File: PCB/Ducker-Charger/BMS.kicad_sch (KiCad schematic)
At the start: 26 parts, among them Q5 NCE3080K, Q6 NCE3080K, U4 BQ7791500PWR

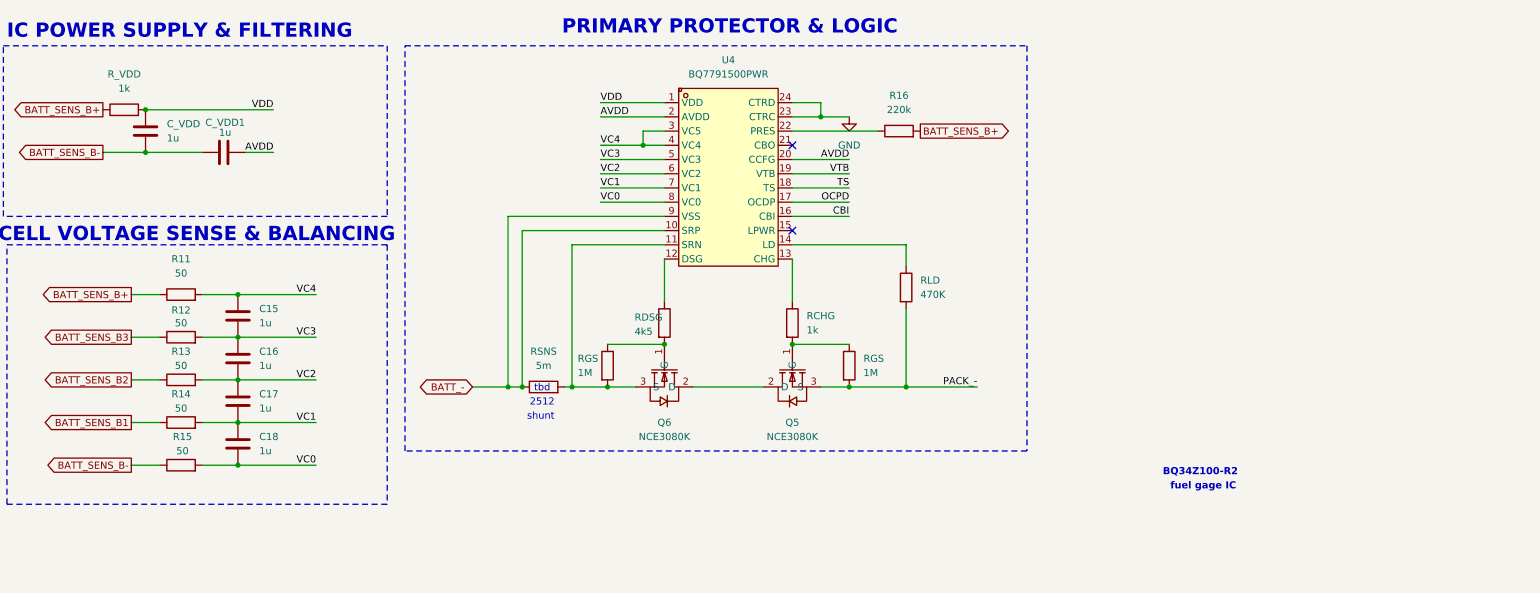
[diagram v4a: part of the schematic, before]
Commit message: fix: placement and values
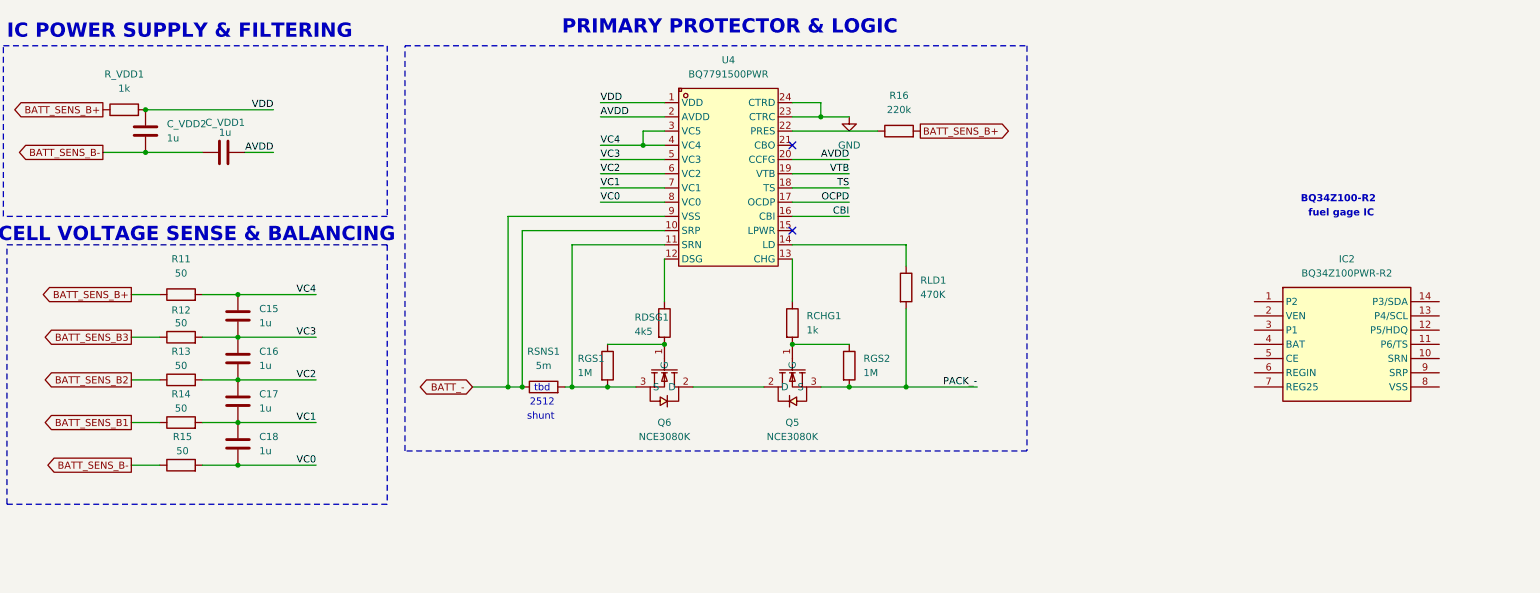
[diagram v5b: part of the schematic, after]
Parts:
- added IC2: BQ34Z100PWR-R2, SOP65P640X120-14N, symbol BQ34Z100PWR-R2:BQ34Z100PWR-R2
- renumbered C_VDD to C_VDD2, RCHG to RCHG1, RDSG to RDSG1, RGS to RGS1, RGS to RGS2, RLD to RLD1, RSNS to RSNS1, R_VDD to R_VDD1
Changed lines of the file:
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@@
 	(text "BQ34Z100-R2"
 		(exclude_from_sim no)
-		(at 229.108 107.95 0)
+		(at 253.746 59.182 0)
 		(effects
 			(font
@@
 	(text "fuel gage IC\n"
 		(exclude_from_sim no)
-		(at 229.616 110.49 0)
+		(at 254.254 61.722 0)
 		(effects
 			(font
@@
 		(dnp no)
 		(fields_autoplaced yes)
-		(property "Reference" "RSNS"
+		(property "Reference" "RSNS1"
 			(at 111.76 86.36 90)
 			(effects
@@
 			(project ""
 				(path "/74790d6c-a68e-4e6d-b4a9-43de1843f817/2619d069-74ef-4c2a-996f-0b2ab6b3180e"
-					(reference "RSNS")
+					(reference "RSNS1")
 					(unit 1)
 				)
@@
 		(dnp no)
 		(fields_autoplaced yes)
-		(property "Reference" "RGS"
+		(property "Reference" "RGS2"
 			(at 168.91 87.6299 0)
 			(effects
@@
 			(project "Ducker-Charger"
 				(path "/74790d6c-a68e-4e6d-b4a9-43de1843f817/2619d069-74ef-4c2a-996f-0b2ab6b3180e"
-					(reference "RGS")
+					(reference "RGS2")
 					(unit 1)
 				)
@@
 		(on_board yes)
 		(dnp no)
-		(property "Reference" "RDSG"
+		(property "Reference" "RDSG1"
 			(at 128.016 80.264 0)
 			(effects
@@
 			(project "Ducker-Charger"
 				(path "/74790d6c-a68e-4e6d-b4a9-43de1843f817/2619d069-74ef-4c2a-996f-0b2ab6b3180e"
-					(reference "RDSG")
+					(reference "RDSG1")
 					(unit 1)
 				)
@@
 		(dnp no)
 		(fields_autoplaced yes)
-		(property "Reference" "C_VDD"
+		(property "Reference" "C_VDD2"
 			(at 44.45 45.7199 0)
 			(effects
@@
 			(project "Ducker-Charger"
 				(path "/74790d6c-a68e-4e6d-b4a9-43de1843f817/2619d069-74ef-4c2a-996f-0b2ab6b3180e"
-					(reference "C_VDD")
+					(reference "C_VDD2")
 					(unit 1)
 				)
@@
 		(dnp no)
 		(fields_autoplaced yes)
-		(property "Reference" "RLD"
+		(property "Reference" "RLD1"
 			(at 179.07 73.6599 0)
 			(effects
@@
 			(project ""
 				(path "/74790d6c-a68e-4e6d-b4a9-43de1843f817/2619d069-74ef-4c2a-996f-0b2ab6b3180e"
-					(reference "RLD")
+					(reference "RLD1")
 					(unit 1)
 				)
@@
 		(dnp no)
 		(fields_autoplaced yes)
-		(property "Reference" "R_VDD"
+		(property "Reference" "R_VDD1"
 			(at 36.83 36.83 90)
 			(effects
@@
 			(project "Ducker-Charger"
 				(path "/74790d6c-a68e-4e6d-b4a9-43de1843f817/2619d069-74ef-4c2a-996f-0b2ab6b3180e"
-					(reference "R_VDD")
+					(reference "R_VDD1")
 					(unit 1)
 				)
@@
 	)
 	(symbol
+		(lib_id "BQ34Z100PWR-R2:BQ34Z100PWR-R2")
+		(at 238.76 77.47 0)
+		(unit 1)
+		(exclude_from_sim no)
+		(in_bom yes)
+		(on_board yes)
+		(dnp no)
+		(fields_autoplaced yes)
+		(property "Reference" "IC2"
+			(at 255.27 69.85 0)
+			(effects
+				(font
+					(size 1.27 1.27)
+				)
+			)
+		)
+		(property "Value" "BQ34Z100PWR-R2"
+			(at 255.27 72.39 0)
+			(effects
+				(font
+					(size 1.27 1.27)
+				)
+			)
+		)
+		(property "Footprint" "SOP65P640X120-14N"
+			(at 267.97 172.39 0)
+			(effects
+				(font
+					(size 1.27 1.27)
+				)
+				(justify left top)
+				(hide yes)
+			)
+		)
+		(property "Datasheet" "kicad-embed://bq34z100-r2.pdf"
+			(at 267.97 272.39 0)
+			(effects
+				(font
+					(size 1.27 1.27)
+				)
+				(justify left top)
+				(hide yes)
+			)
+		)
+		(property "Description" "Battery Management Multi-chemistry Impedance Track stand-alone fuel gauge"
+			(at 238.76 77.47 0)
+			(effects
+				(font
+					(size 1.27 1.27)
+				)
+				(hide yes)
+			)
+		)
+		(property "Height" "1.2"
+			(at 267.97 472.39 0)
+			(effects
+				(font
+					(size 1.27 1.27)
+				)
+				(justify left top)
+				(hide yes)
+			)
+		)
+		(property "Mouser Part Number" "595-BQ34Z100PWR-R2"
+			(at 267.97 572.39 0)
+			(effects
+				(font
+					(size 1.27 1.27)
+				)
+				(justify left top)
+				(hide yes)
+			)
+		)
+		(property "Mouser Price/Stock" "https://www.mouser.co.uk/ProductDetail/Texas-Instruments/BQ34Z100PWR-R2?qs=rQFj71Wb1eWspkgmxcmVcA%3D%3D"
+			(at 267.97 672.39 0)
+			(effects
+				(font
+					(size 1.27 1.27)
+				)
+				(justify left top)
+				(hide yes)
+			)
+		)
+		(property "Manufacturer_Name" "Texas Instruments"
+			(at 267.97 772.39 0)
+			(effects
+				(font
+					(size 1.27 1.27)
+				)
+				(justify left top)
+				(hide yes)
+			)
+		)
+		(property "Manufacturer_Part_Number" "BQ34Z100PWR-R2"
+			(at 267.97 872.39 0)
+			(effects
+				(font
+					(size 1.27 1.27)
+				)
+				(justify left top)
+				(hide yes)
+			)
+		)
+		(pin "9"
+		)
+		(pin "12"
+		)
+		(pin "14"
+		)
+		(pin "6"
+		)
+		(pin "1"
+		)
+		(pin "3"
+		)
+		(pin "4"
+		)
+		(pin "2"
+		)
+		(pin "5"
+		)
+		(pin "7"
+		)
+		(pin "10"
+		)
+		(pin "13"
+		)
+		(pin "11"
+		)
+		(pin "8"
+		)
+		(instances
+			(project ""
+				(path "/74790d6c-a68e-4e6d-b4a9-43de1843f817/2619d069-74ef-4c2a-996f-0b2ab6b3180e"
+					(reference "IC2")
+					(unit 1)
+				)
+			)
+		)
+	)
+	(symbol
 		(lib_id "Device:R")
 		(at 137.16 175.26 0)
@@
 		(dnp no)
 		(fields_autoplaced yes)
-		(property "Reference" "RCHG"
+		(property "Reference" "RCHG1"
 			(at 158.75 80.0099 0)
 			(effects
@@
 			(project "Ducker-Charger"
 				(path "/74790d6c-a68e-4e6d-b4a9-43de1843f817/2619d069-74ef-4c2a-996f-0b2ab6b3180e"
-					(reference "RCHG")
+					(reference "RCHG1")
 					(unit 1)
 				)
@@
 		(on_board yes)
 		(dnp no)
-		(property "Reference" "RGS"
+		(property "Reference" "RGS1"
 			(at 117.856 87.63 0)
 			(effects
@@
 			(project "Ducker-Charger"
 				(path "/74790d6c-a68e-4e6d-b4a9-43de1843f817/2619d069-74ef-4c2a-996f-0b2ab6b3180e"
-					(reference "RGS")
+					(reference "RGS1")
 					(unit 1)
 				)

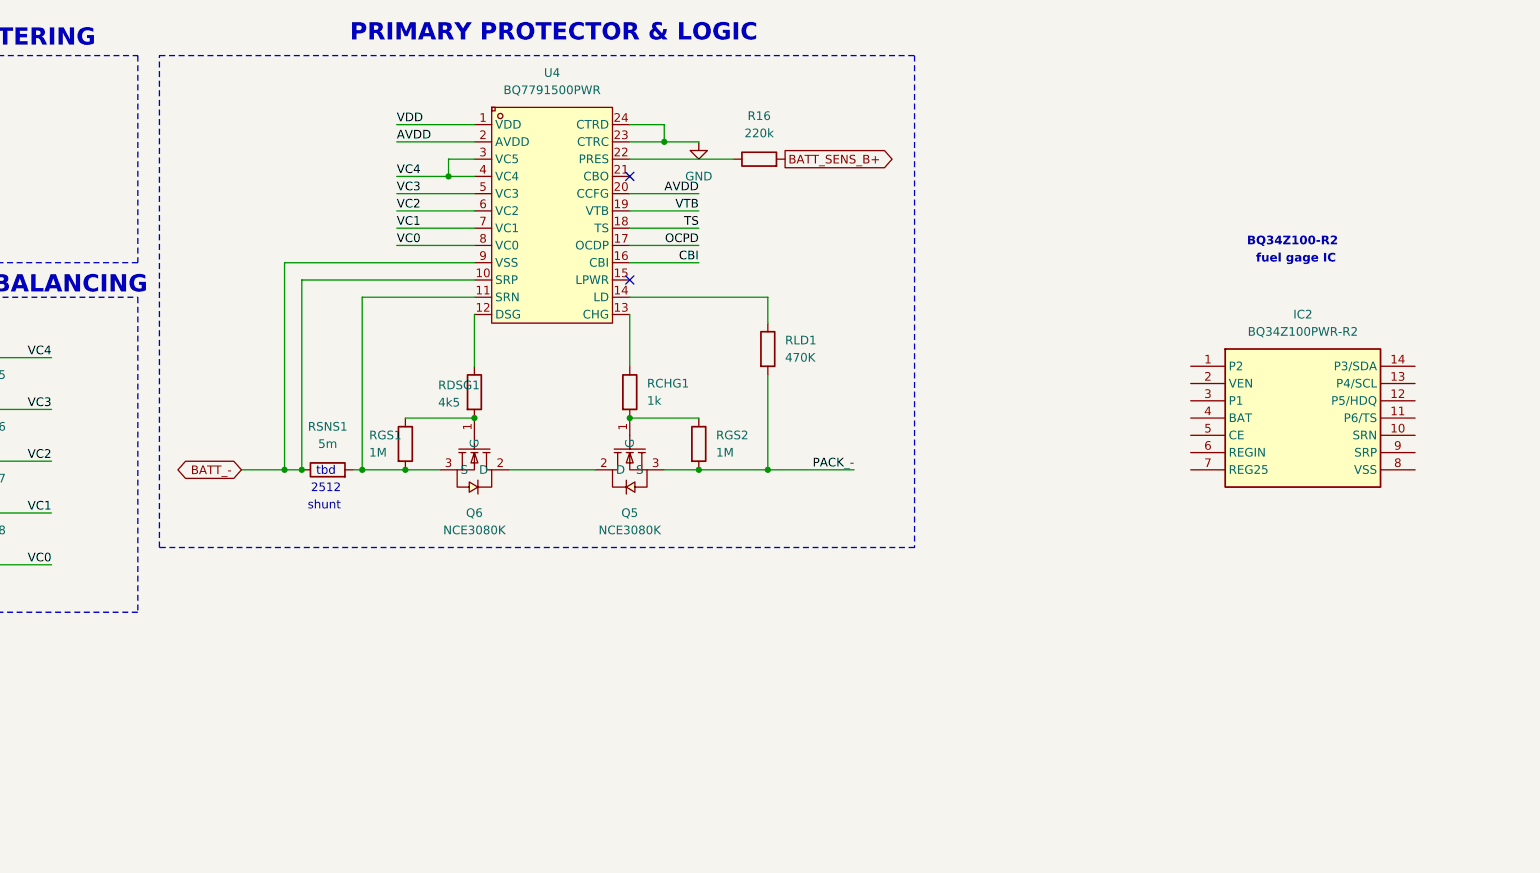
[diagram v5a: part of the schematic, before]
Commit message: feat: completed BMS sheet
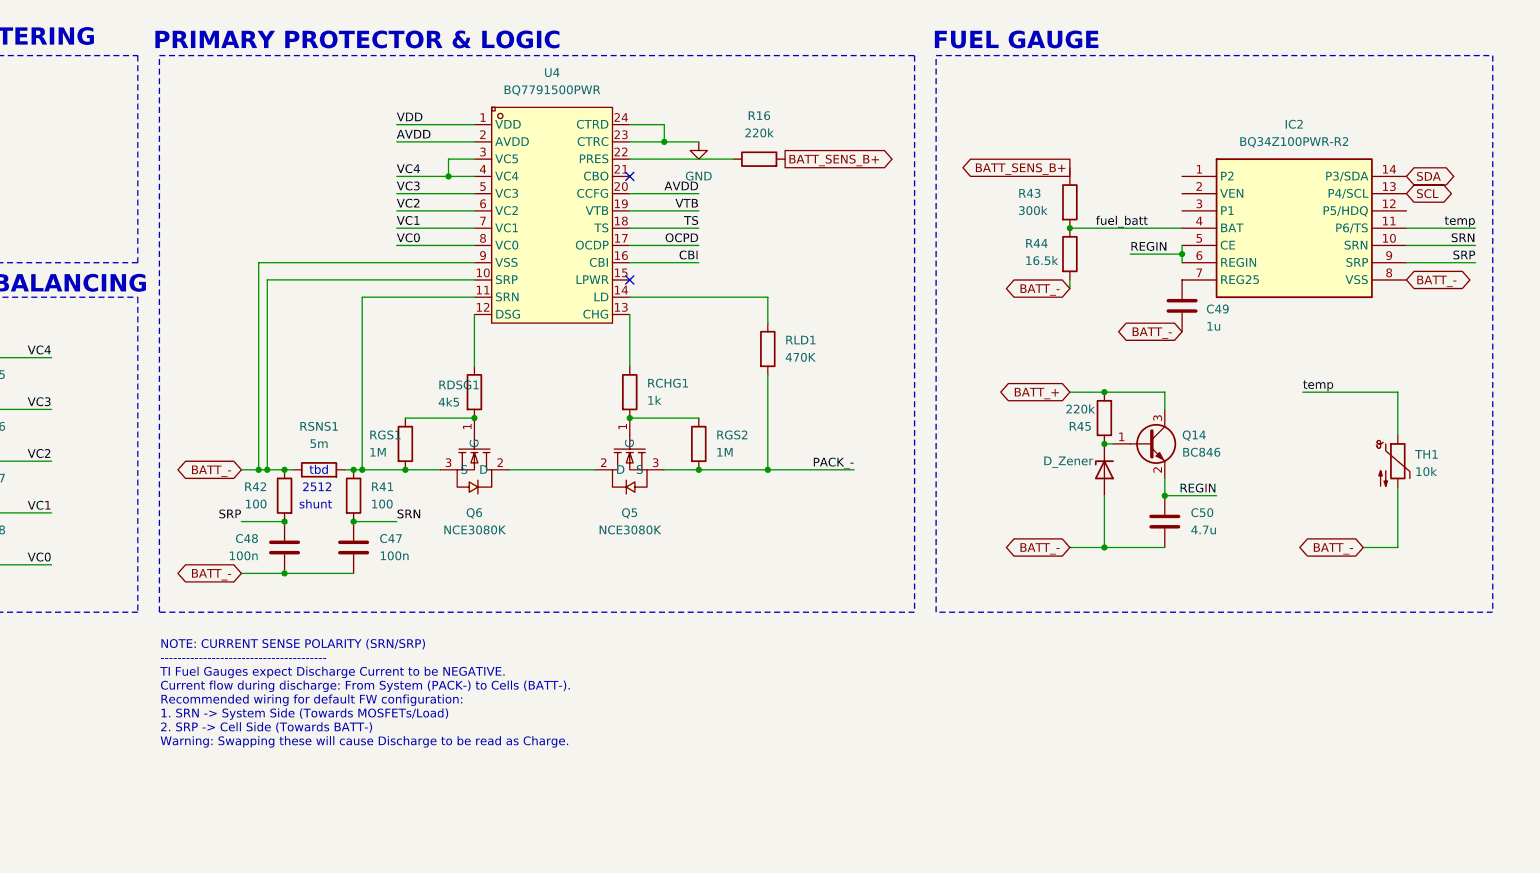
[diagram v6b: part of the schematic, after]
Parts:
- added C47, C48: 100n, symbol Device:C
- added C49: 1u, symbol Device:C
- added C50: 4.7u, symbol Device:C
- added D3: D_Zener, symbol Device:D_Zener
- added Q14: BC846, Package_TO_SOT_SMD:SOT-23, symbol Transistor_BJT:BC846
- added R41, R42: 100, symbol Device:R
- added R43: 300k, symbol Device:R
- added R44: 16.5k, symbol Device:R
- added R45: 220k, symbol Device:R
- added TH1: 10k, symbol Device:Thermistor_NTC
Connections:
- net BATT_-: now also IC2.8 (VSS), C47.2, C48.2, C49.2, C50.2, D3.2 (A), R42.1, R44.2, TH1.2
- net BATT_SENS_B+: now also R43.1
- net at Q6.3 (S), RGS1.2, RSNS1.2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: now also R41.1
- net SRN: now reaches IC2.10 (SRN)
- net SRN: now also C47.1, R41.2
- net temp: now reaches IC2.11 (P6/TS)
- net temp: now also TH1.1
- net SCL: now reaches IC2.13 (P4/SCL)
- net SDA: now reaches IC2.14 (P3/SDA)
- net fuel_batt: now reaches IC2.4 (BAT)
- net fuel_batt: now also R43.2, R44.1
- net REGIN: now reaches IC2.5 (CE)
- net REGIN: now also IC2.6 (REGIN), C50.1, Q14.2 (E)
- net at IC2.7 (REG25): now also C49.1
- net SRP: now reaches IC2.9 (SRP)
- net SRP: now also C48.1, R42.2
- new net: D3.1 (K), Q14.1 (B), R45.1
- new net BATT_+: Q14.3 (C), R45.2
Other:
- note added: "FUEL GAUGE"
- note added: "NOTE: CURRENT SENSE POLARITY (SRN/SRP) --------------------------------------- TI Fuel Gauges expect Discharge Current to be NEGATIVE. Current flow during discharge: From System (PACK-) to Cells (BATT-). Recommended wiring for default FW configuration: 1. SRN -> System Side (Towards MOSFETs/Load) 2. SRP -> Cell Side (Towards BATT-) Warning: Swapping these will cause Discharge to be read as Charge."
- note removed: "BQ34Z100-R2"
- note removed: "fuel gage IC"
- moved on the sheet: IC2, RSNS1
